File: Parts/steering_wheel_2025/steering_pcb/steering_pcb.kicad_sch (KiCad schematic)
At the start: 28 parts, among them J0 Quick_connector, J15 CAN pin header, SW1 Push_Button, U2 TPS5430DDA, U3 TPS5430DDA

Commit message: pcb progress backup
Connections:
- net button7_0: now also A1.D13
- net button7_1: now also A1.D11
- net button7_2: now also A1.D12
- net button7_3: now also A1.D10
- net button8_0: now also A1.D9
- net button8_1: now also A1.D8
- net button8_2: now also A1.D7
- net button8_3: now also A1.D6
- net button9_0: now also A1.D5
- net button9_1: now also A1.D3 (D3_INT1)
- net button9_2: now also A1.D4
- net button9_3: now also A1.D14 (D14/TX3)
- no-connect marks 19 -> 17

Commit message: PCB v1
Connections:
- net button10_0: now also A1.D1 (D1/TX0)
- net button10_1: now also A1.D15 (D15/RX3)
- net button10_2: now also A1.D16 (D16/TX2)
- net button10_3: now also A1.D17 (D17/RX2)
- net button11_0: now also A1.D18 (D18/TX1)
- net button11_1: now also A1.D20 (D20/SDA)
- net button11_2: now also A1.D19 (D19/RX1)
- net button11_3: now also A1.D21 (D21/SCL)
- net button5_2: now also A1.D52 (D52_SCK); no longer A1.D48
- net button5_3: now also A1.D48; no longer A1.D52 (D52_SCK)
- no-connect marks 17 -> 9

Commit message: KiCad after review 1
Spinat skal hjem og gro, Ost tager over og arbejder videre efter hans gode første review.
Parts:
- added J14: Conn_01x04_Pin, Connector_PinHeader_1.00mm:PinHeader_1x04_P1.00mm_Vertical, symbol Connector:Conn_01x04_Pin
- added J16: Conn_01x01_Pin, Connector_PinSocket_2.00mm:PinSocket_1x01_P2.00mm_Vertical, symbol Connector:Conn_01x01_Pin
- added R86, R87, R88, R89: 10k, Resistor_SMD:R_0402_1005Metric_Pad0.72x0.64mm_HandSolder, symbol Device:R_Small
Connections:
- net +5V_MCU: now also J16.1 (Pin_1)
- net GND: now also R86.1, R87.1, R88.1, R89.1
- net LED_PWM_controller: now also A1.D27; no longer A1.D23
- net button12_0: now also A1.D23
- net button12_1: now also A1.D24
- net button12_2: now also A1.D22
- net button12_3: now also A1.D25
- net at A1.D30: now also J14.4 (Pin_4), R86.2
- net at A1.D31: now also J14.3 (Pin_3), R87.2
- net at A1.D32: now also J14.2 (Pin_2), R88.2
- net at A1.D33: now also J14.1 (Pin_1), R89.2

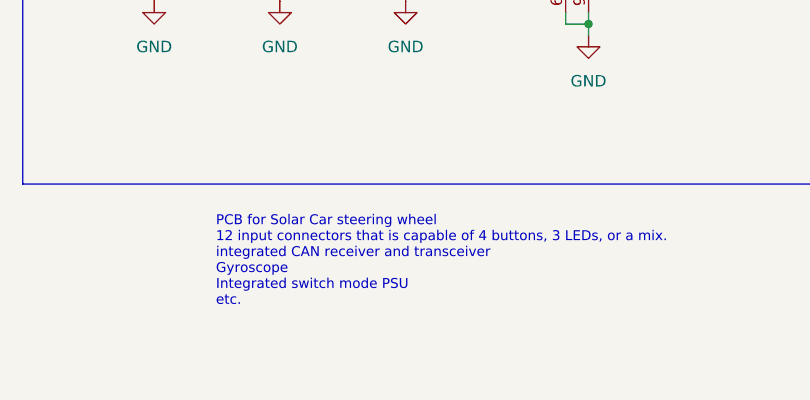
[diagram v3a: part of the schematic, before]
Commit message: slight changes in schematic
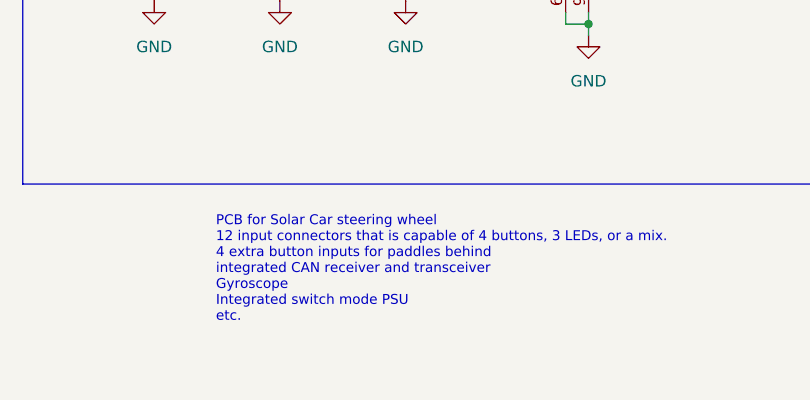
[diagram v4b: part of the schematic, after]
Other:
- note added: "PCB for Solar Car steering wheel 12 input connectors that is capable of 4 buttons, 3 LEDs, or a mix. 4 extra button inputs for paddles behind integrated CAN receiver and transceiver Gyroscope Integrated switch mode PSU etc."
- note removed: "PCB for Solar Car steering wheel 12 input connectors that is capable of 4 buttons, 3 LEDs, or a mix. integrated CAN receiver and transceiver Gyroscope Integrated switch mode PSU etc."
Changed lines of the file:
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@@
 		)
 	)
-	(text "PCB for Solar Car steering wheel\n12 input connectors that is capable of 4 buttons, 3 LEDs, or a mix.\nintegrated CAN receiver and transceiver\nGyroscope\nIntegrated switch mode PSU\netc."
+	(text "PCB for Solar Car steering wheel\n12 input connectors that is capable of 4 buttons, 3 LEDs, or a mix.\n4 extra button inputs for paddles behind\nintegrated CAN receiver and transceiver\nGyroscope\nIntegrated switch mode PSU\netc."
 		(exclude_from_sim no)
 		(at 178.308 167.386 0)

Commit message: PCB work update
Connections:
- net CAN_H: now also J0.2; no longer J0.4
- net CAN_L: now also J0.4; no longer J0.2
- net at A1.D34: now also J14.4 (Pin_4), R89.2
- net at A1.D36: now also J14.3 (Pin_3), R88.2
- net at A1.D38: now also J14.2 (Pin_2), R87.2
- net at A1.D40: now also J14.1 (Pin_1), R86.2
- now unconnected: A1.D30, A1.D31, A1.D32, A1.D33

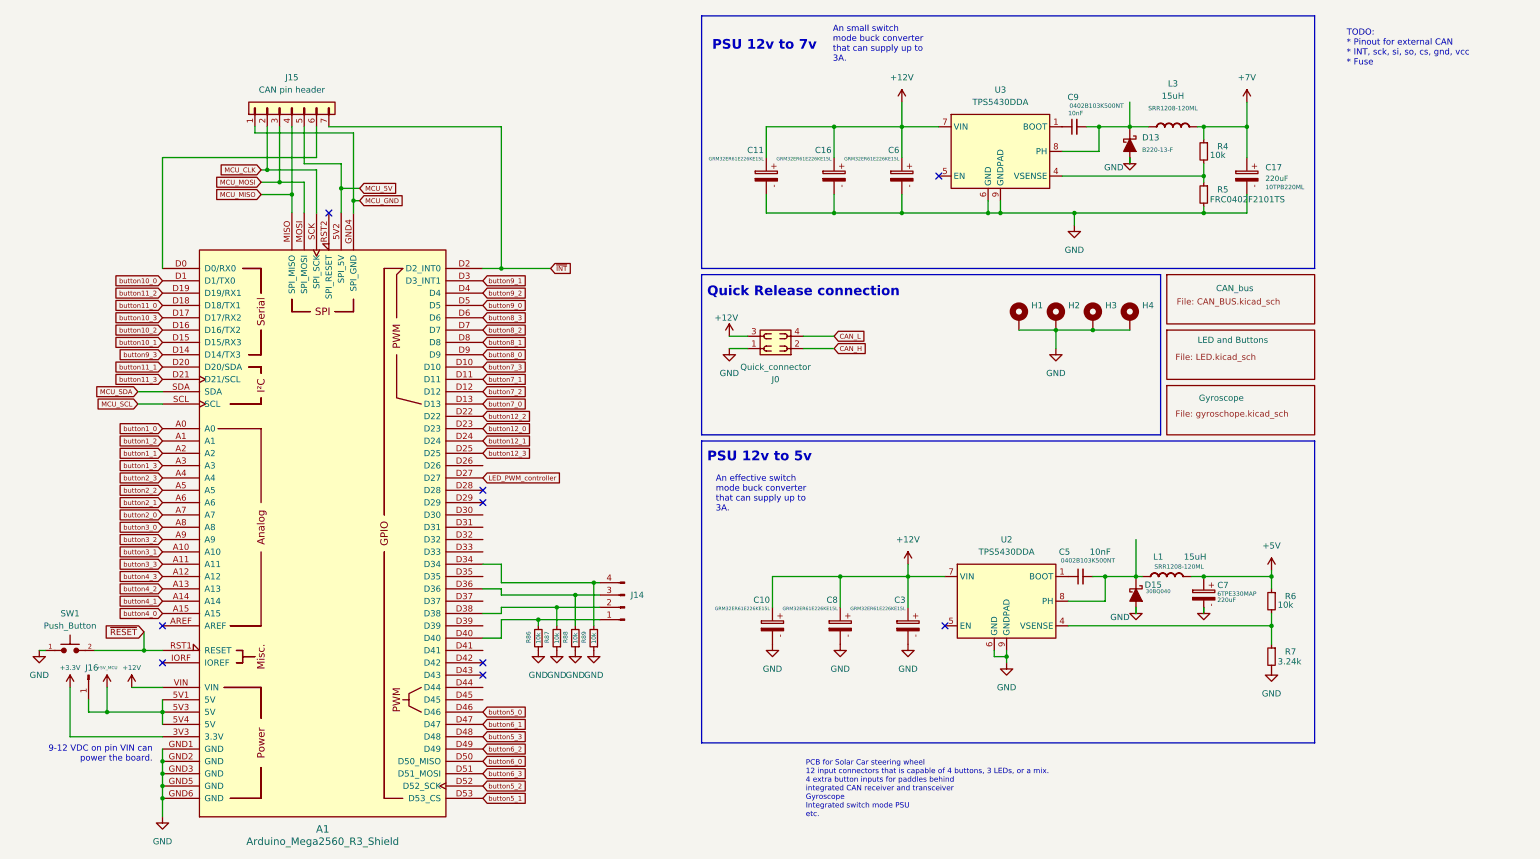
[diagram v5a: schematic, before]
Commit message: Error fixing with kicad_dru, and silkscreeen updates. TO-DO: BOM to basic
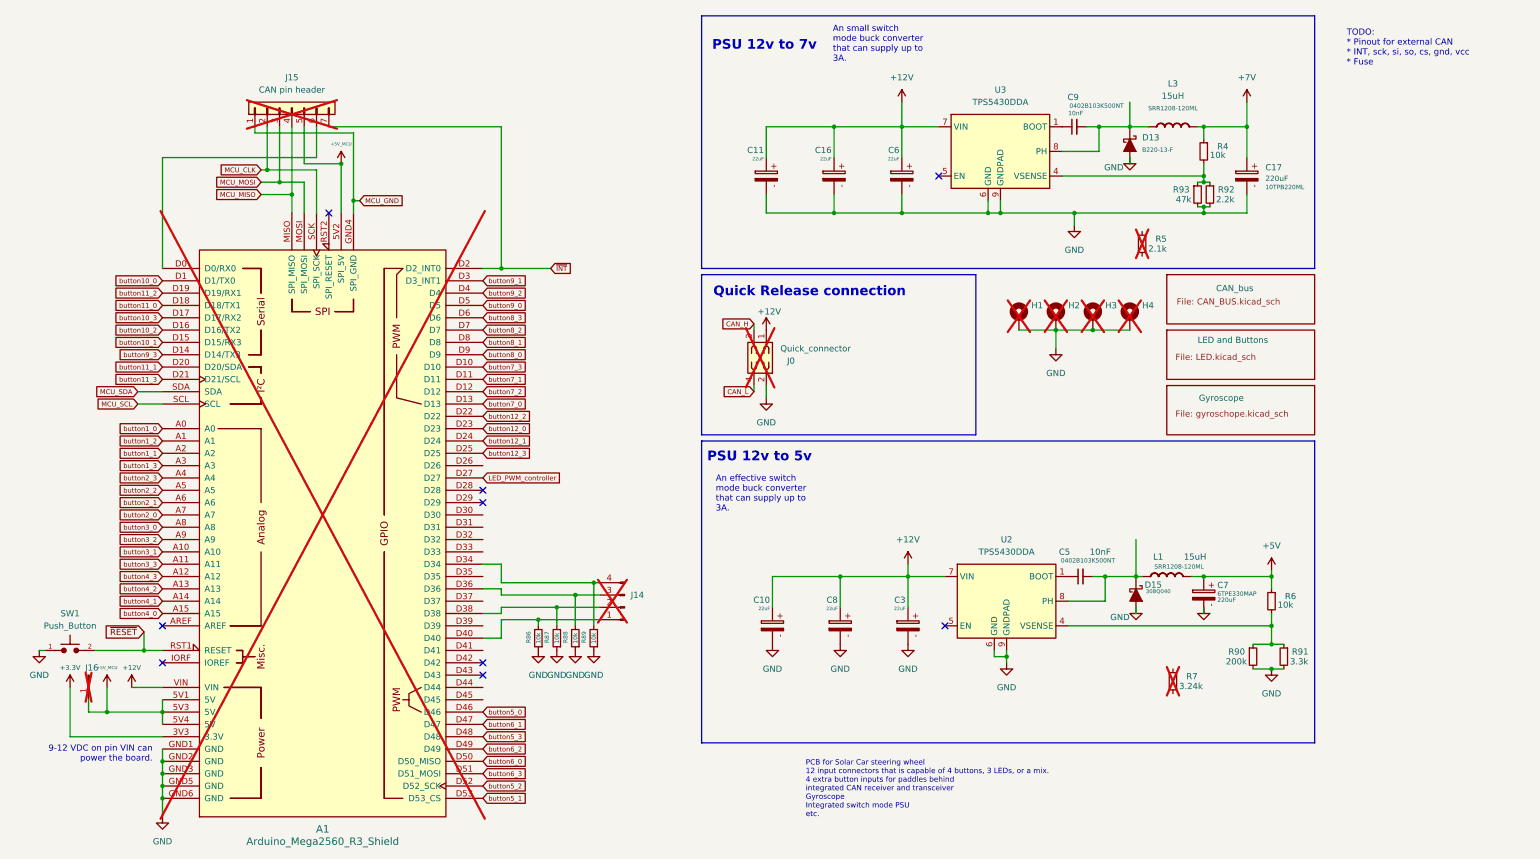
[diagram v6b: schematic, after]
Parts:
- added R90: 200k, Resistor_SMD:R_0402_1005Metric_Pad0.72x0.64mm_HandSolder, symbol Device:R_Small
- added R91: 3.3k, Resistor_SMD:R_0402_1005Metric_Pad0.72x0.64mm_HandSolder, symbol Device:R_Small
- added R92: 2.2k, Resistor_SMD:R_0402_1005Metric_Pad0.72x0.64mm_HandSolder, symbol Device:R_Small
- added R93: 47k, Resistor_SMD:R_0402_1005Metric_Pad0.72x0.64mm_HandSolder, symbol Device:R_Small
- A1, H1, H2, H3, H4, J15, J16: now not fitted
- C10, C11, C16, C3, C6, C8: value GRM32ER61E226KE15L -> 22uF; footprint Capacitor_SMD:C_1210_3225Metric_Pad1.33x2.70mm_HandSolder -> Capacitor_SMD:C_1206_3216Metric_Pad1.33x1.80mm_HandSolder; JLCPCB C699521 -> C12891; Note (none) -> basic
- J0: footprint Connector_PinSocket_2.54mm:PinSocket_2x02_P2.54mm_Vertical -> Connector_Molex:Molex_Micro-Fit_3.0_43045-0412_2x02_P3.00mm_Vertical; now not fitted
- J14: footprint Connector_PinHeader_1.00mm:PinHeader_1x04_P1.00mm_Vertical -> Connector_PinHeader_2.54mm:PinHeader_1x04_P2.54mm_Vertical; now not fitted
- R4, R6, R86, R87, R88, R89: Note (none) -> basic
- R5: value FRC0402F2101TS -> 2.1k; now not fitted; now left out of the parts list
- R7: now not fitted; now left out of the parts list
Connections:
- net MCU_5V is gone; now on net +5V_MCU: A1.5V2 (SPI_5V), J15.5
- net +12V: now also J0.1; no longer J0.3
- net CAN_H: now also J0.3; no longer J0.2
- net GND: now also J0.2, R90.2, R91.2, R92.2, R93.2; no longer J0.1, R5.2, R7.2
- net at R6.2, U2.4 (VSENSE): now also R90.1, R91.1; no longer R7.1
- net at R4.2, U3.4 (VSENSE): now also R92.1, R93.1; no longer R5.1

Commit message: board update
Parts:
- removed R7: 3.24k, Resistor_SMD:R_0402_1005Metric_Pad0.72x0.64mm_HandSolder, symbol Device:R_Small
- added D18, D19: ~, Diode_SMD:D_SMA, symbol PCM_Diode_Schottky_AKL:B340
- added F1: Fuse, symbol Device:Fuse
- C10, C11, C16, C3, C6, C8: Product (none) -> CL31A226KAHNNNE
- C17: value 10TPB220ML -> 220uF; footprint PCM_Capacitor_Tantalum_SMD_AKL:CAP_10TPB220ML -> ROAST:CAP_10TPB220ML; Note (none) -> no; Product https://jlcpcb.com/partdetail/Panasonic-10TPB220ML/C347545 -> 10TPB220ML
- C5, C9: JLCPCB C1524 -> C1710; Note (none) -> basic; Product (none) -> CL21B103KBANNNC
- C7: value 220uF -> 330uF; JLCPCB C3340 -> C79112; Note (none) -> no; Product https://www.lcsc.com/product-detail/Aluminum-Electrolytic-C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 -> 6TPE330MAP
- D13: value B220-13-F -> ~; Product (none) -> B220-13-F; now not fitted; now left out of the parts list
- D15: value 30BQ040 -> ~; Product (none) -> 30BQ040; now not fitted; now left out of the parts list
- L1, L3: Note (none) -> no; Product (none) -> SRR1208-120ML
- R4, R6, R86, R87, R88, R89: Product (none) -> 0402WGJ0103TCE
- R90: Product (none) -> 0402WGF2003TCE
- R91: Product (none) -> 0402WGF3301TCE
- R92: Product (none) -> 0402WGF2201TCE
- R93: Product (none) -> 0402WGF4702TCE
- SW1: now not fitted
- U2, U3: Note (none) -> basic
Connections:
- net +12V: now also U3.1 (BOOT), F1.2; no longer J0.1, U3.7 (VIN)
- net GND: now also D18.2 (A), D19.2 (A); no longer D13.2 (A), D15.2 (A), U3.6 (GND)
- net at C5.2, L1.1 (+), U2.8 (PH): now also D19.1 (K); no longer D15.1 (K)
- net at C9.2, L3.1 (+): now also D18.1 (K); no longer D13.1 (K), U3.8 (PH)
- net at C9.1: now also U3.7 (VIN); no longer U3.1 (BOOT)
- net at R4.2, R92.1, R93.1: now also U3.5 (EN); no longer U3.4 (VSENSE)
- new net: F1.1, J0.1
- no-connect marks 9 -> 19
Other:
- note added: "(expensive, more effective alternative)"
- moved on the sheet: R5, R90, R91

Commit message: Rename folders for consistency
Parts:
- D18, D19: value ~ -> SS34
- R4, R6, R86, R87, R88, R89: value 10k -> 10kΩ
- R90: value 200k -> 200kΩ
- R91: value 3.3k -> 3.3kΩ
- R92: value 2.2k -> 2.2kΩ
- R93: value 47k -> 47kΩ
- U2, U3: value TPS5430DDA -> TPS5430DDAR
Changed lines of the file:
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@@
 (kicad_sch
-	(version 20231120)
+	(version 20250114)
 	(generator "eeschema")
-	(generator_version "8.0")
+	(generator_version "9.0")
 	(paper "A4")
 	(title_block
@@
 		(company "DTU ROAST")
 	)
+	(rectangle
+		(start 156.845 101.6)
+		(end 283.21 163.83)
+		(stroke
+			(width 0)
+			(type default)
+		)
+		(fill
+			(type none)
+		)
+	)
+	(rectangle
+		(start 247.65 13.97)
+		(end 278.13 24.13)
+		(stroke
+			(width 0)
+			(type default)
+		)
+		(fill
+			(type none)
+		)
+	)
+	(rectangle
+		(start 156.845 67.31)
+		(end 213.36 100.33)
+		(stroke
+			(width 0)
+			(type default)
+		)
+		(fill
+			(type none)
+		)
+	)
+	(rectangle
+		(start 156.845 12.7)
+		(end 283.21 66.04)
+		(stroke
+			(width 0)
+			(type default)
+		)
+		(fill
+			(type none)
+		)
+	)
+	(rectangle
+		(start 251.46 102.87)
+		(end 281.94 113.03)
+		(stroke
+			(width 0)
+			(type default)
+		)
+		(fill
+			(type none)
+		)
+	)
+	(text "9-12 VDC on pin VIN can\npower the board."
+		(exclude_from_sim no)
+		(at 43.688 166.116 0)
+		(effects
+			(font
+				(size 1.27 1.27)
+			)
+			(justify right)
+		)
+	)
+	(text "PSU 12v to 7v"
+		(exclude_from_sim no)
+		(at 159.004 20.066 0)
+		(effects
+			(font
+				(size 2 2)
+				(thickness 0.4)
+				(bold yes)
+			)
+			(justify left)
+		)
+	)
+	(text "TODO:\n* Pinout for external CAN\n* INT, sck, si, so, cs, gnd, vcc\n* Fuse"
+		(exclude_from_sim no)
+		(at 289.814 20.574 0)
+		(effects
+			(font
+				(size 1.27 1.27)
+			)
+			(justify left)
+		)
+	)
+	(text "(expensive, more\neffective alternative)"
+		(exclude_from_sim no)
+		(at 260.35 17.78 0)
+		(effects
+			(font
+				(size 1 1)
+			)
+			(justify left)
+		)
+	)
+	(text "(expensive, more\neffective alternative)"
+		(exclude_from_sim no)
+		(at 264.16 106.68 0)
+		(effects
+			(font
+				(size 1 1)
+			)
+			(justify left)
+		)
+	)
+	(text "An small switch\nmode buck converter\nthat can supply up to\n3A."
+		(exclude_from_sim no)
+		(at 183.896 19.812 0)
+		(effects
+			(font
+				(size 1.27 1.27)
+			)
+			(justify left)
+		)
+	)
+	(text "PCB for Solar Car steering wheel\n12 input connectors that is capable of 4 buttons, 3 LEDs, or a mix.\n4 extra button inputs for paddles behind\nintegrated CAN receiver and transceiver\nGyroscope\nIntegrated switch mode PSU\netc."
+		(exclude_from_sim no)
+		(at 178.308 167.386 0)
+		(effects
+			(font
+				(size 1.1 1.1)
+			)
+			(justify left top)
+		)
+	)
+	(text "An effective switch\nmode buck converter\nthat can supply up to\n3A."
+		(exclude_from_sim no)
+		(at 159.766 112.522 0)
+		(effects
+			(font
+				(size 1.27 1.27)
+			)
+			(justify left)
+		)
+	)
+	(text "Quick Release connection"
+		(exclude_from_sim no)
+		(at 159.258 70.866 0)
+		(effects
+			(font
+				(size 2 2)
+				(thickness 0.4)
+				(bold yes)
+			)
+			(justify left)
+		)
+	)
+	(text "PSU 12v to 5v"
+		(exclude_from_sim no)
+		(at 157.988 104.902 0)
+		(effects
+			(font
+				(size 2 2)
+				(thickness 0.4)
+				(bold yes)
+			)
+			(justify left)
+		)
+	)
 	(junction
 		(at 233.68 54.61)
@@
 		)
 	)
-	(rectangle
-		(start 156.845 101.6)
-		(end 283.21 163.83)
-		(stroke
-			(width 0)
-			(type default)
-		)
-		(fill
-			(type none)
-		)
-	)
-	(rectangle
-		(start 247.65 13.97)
-		(end 278.13 24.13)
-		(stroke
-			(width 0)
-			(type default)
-		)
-		(fill
-			(type none)
-		)
-	)
-	(rectangle
-		(start 156.845 67.31)
-		(end 213.36 100.33)
-		(stroke
-			(width 0)
-			(type default)
-		)
-		(fill
-			(type none)
-		)
-	)
-	(rectangle
-		(start 156.845 12.7)
-		(end 283.21 66.04)
-		(stroke
-			(width 0)
-			(type default)
-		)
-		(fill
-			(type none)
-		)
-	)
-	(rectangle
-		(start 251.46 102.87)
-		(end 281.94 113.03)
-		(stroke
-			(width 0)
-			(type default)
-		)
-		(fill
-			(type none)
-		)
-	)
 	(image
 		(at 201.295 86.995)
@@
 		)
 	)
-	(text "9-12 VDC on pin VIN can\npower the board."
-		(exclude_from_sim no)
-		(at 43.688 166.116 0)
-		(effects
-			(font
-				(size 1.27 1.27)
-			)
-			(justify right)
-		)
-	)
-	(text "PSU 12v to 7v"
-		(exclude_from_sim no)
-		(at 159.004 20.066 0)
-		(effects
-			(font
-				(size 2 2)
-				(thickness 0.4)
-				(bold yes)
-			)
-			(justify left)
-		)
-	)
-	(text "TODO:\n* Pinout for external CAN\n* INT, sck, si, so, cs, gnd, vcc\n* Fuse"
-		(exclude_from_sim no)
-		(at 289.814 20.574 0)
-		(effects
-			(font
-				(size 1.27 1.27)
-			)
-			(justify left)
-		)
-	)
-	(text "(expensive, more\neffective alternative)"
-		(exclude_from_sim no)
-		(at 260.35 17.78 0)
-		(effects
-			(font
-				(size 1 1)
-			)
-			(justify left)
-		)
-	)
-	(text "(expensive, more\neffective alternative)"
-		(exclude_from_sim no)
-		(at 264.16 106.68 0)
-		(effects
-			(font
-				(size 1 1)
-			)
-			(justify left)
-		)
-	)
-	(text "An small switch\nmode buck converter\nthat can supply up to\n3A."
-		(exclude_from_sim no)
-		(at 183.896 19.812 0)
-		(effects
-			(font
-				(size 1.27 1.27)
-			)
-			(justify left)
-		)
-	)
-	(text "PCB for Solar Car steering wheel\n12 input connectors that is capable of 4 buttons, 3 LEDs, or a mix.\n4 extra button inputs for paddles behind\nintegrated CAN receiver and transceiver\nGyroscope\nIntegrated switch mode PSU\netc."
-		(exclude_from_sim no)
-		(at 178.308 167.386 0)
-		(effects
-			(font
-				(size 1.1 1.1)
-			)
-			(justify left top)
-		)
-	)
-	(text "An effective switch\nmode buck converter\nthat can supply up to\n3A."
-		(exclude_from_sim no)
-		(at 159.766 112.522 0)
-		(effects
-			(font
-				(size 1.27 1.27)
-			)
-			(justify left)
-		)
-	)
-	(text "Quick Release connection"
-		(exclude_from_sim no)
-		(at 159.258 70.866 0)
-		(effects
-			(font
-				(size 2 2)
-				(thickness 0.4)
-				(bold yes)
-			)
-			(justify left)
-		)
-	)
-	(text "PSU 12v to 5v"
-		(exclude_from_sim no)
-		(at 157.988 104.902 0)
-		(effects
-			(font
-				(size 2 2)
-				(thickness 0.4)
-				(bold yes)
-			)
-			(justify left)
-		)
-	)
 	(global_label "MCU_MISO"
 		(shape input)
@@
 			)
 		)
-		(property "Value" "10k"
+		(property "Value" "10kΩ"
 			(at 275.59 135.382 0)
 			(effects
@@
 			)
 		)
-		(property "Value" "10k"
+		(property "Value" "10kΩ"
 			(at 134.62 142.24 90)
 			(effects
@@
 			)
 		)
-		(property "Value" "10k"
+		(property "Value" "10kΩ"
 			(at 130.81 142.24 90)
 			(effects
@@
 			)
 		)
-		(property "Value" "~"
+		(property "Value" "SS34"
 			(at 248.92 134.3025 90)
 			(effects
@@
 			)
 		)
-		(property "Value" "TPS5430DDA"
+		(property "Value" "TPS5430DDAR"
 			(at 218.44 31.75 0)
 			(effects
@@
 			)
 		)
-		(property "Value" "200k"
+		(property "Value" "200kΩ"
 			(at 271.78 147.066 0)
 			(effects
@@
 			)
 		)
-		(property "Value" "10k"
+		(property "Value" "10kΩ"
 			(at 127 142.24 90)
 			(effects
@@
 			)
 		)
-		(property "Value" "10k"
+		(property "Value" "10kΩ"
 			(at 123.19 142.24 90)
 			(effects
@@
 			)
 		)
-		(property "Value" "47k"
+		(property "Value" "47kΩ"
 			(at 257.81 51.816 0)
 			(effects
@@
 			)
 		)
-		(property "Value" "~"
+		(property "Value" "SS34"
 			(at 247.65 41.5925 90)
 			(effects
@@
 			)
 		)
-		(property "Value" "10k"
+		(property "Value" "10kΩ"
 			(at 261.62 42.672 0)
 			(effects
@@
 			)
 		)
-		(property "Value" "2.2k"
+		(property "Value" "2.2kΩ"
 			(at 262.89 51.816 0)
 			(effects
@@
 			)
 		)
-		(property "Value" "3.3k"
+		(property "Value" "3.3kΩ"
 			(at 276.86 147.066 0)
 			(effects
@@
 			)
 		)
-		(property "Value" "TPS5430DDA"
+		(property "Value" "TPS5430DDAR"
 			(at 219.71 124.46 0)
 			(effects
@@
 		(at 252.73 90.17)
 		(size 30.48 10.16)
+		(exclude_from_sim no)
+		(in_bom yes)
+		(on_board no)
+		(dnp yes)
 		(stroke
 			(width 0.1524)
@@
 		(at 252.73 78.74)
 		(size 30.48 10.16)
+		(exclude_from_sim no)
+		(in_bom yes)
+		(on_board yes)
+		(dnp no)
 		(stroke
 			(width 0.1524)
@@
 		(at 252.73 67.31)
 		(size 30.48 10.16)
+		(exclude_from_sim no)
+		(in_bom yes)
+		(on_board yes)
+		(dnp no)
 		(stroke
 			(width 0.1524)
@@
 		)
 	)
+	(embedded_fonts no)
 )
